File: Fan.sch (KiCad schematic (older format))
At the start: 0 parts

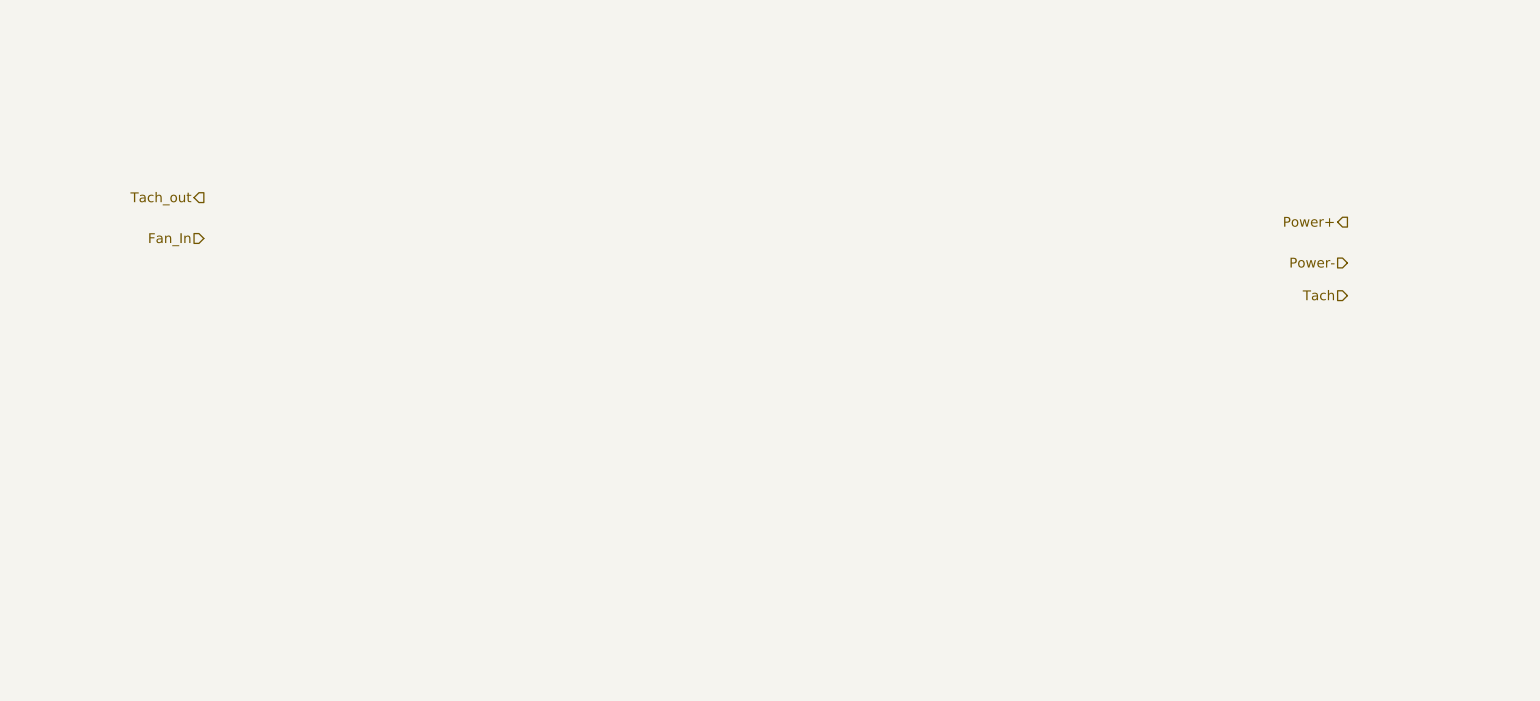
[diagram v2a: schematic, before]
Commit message: Added Fan/Current driver block diagram
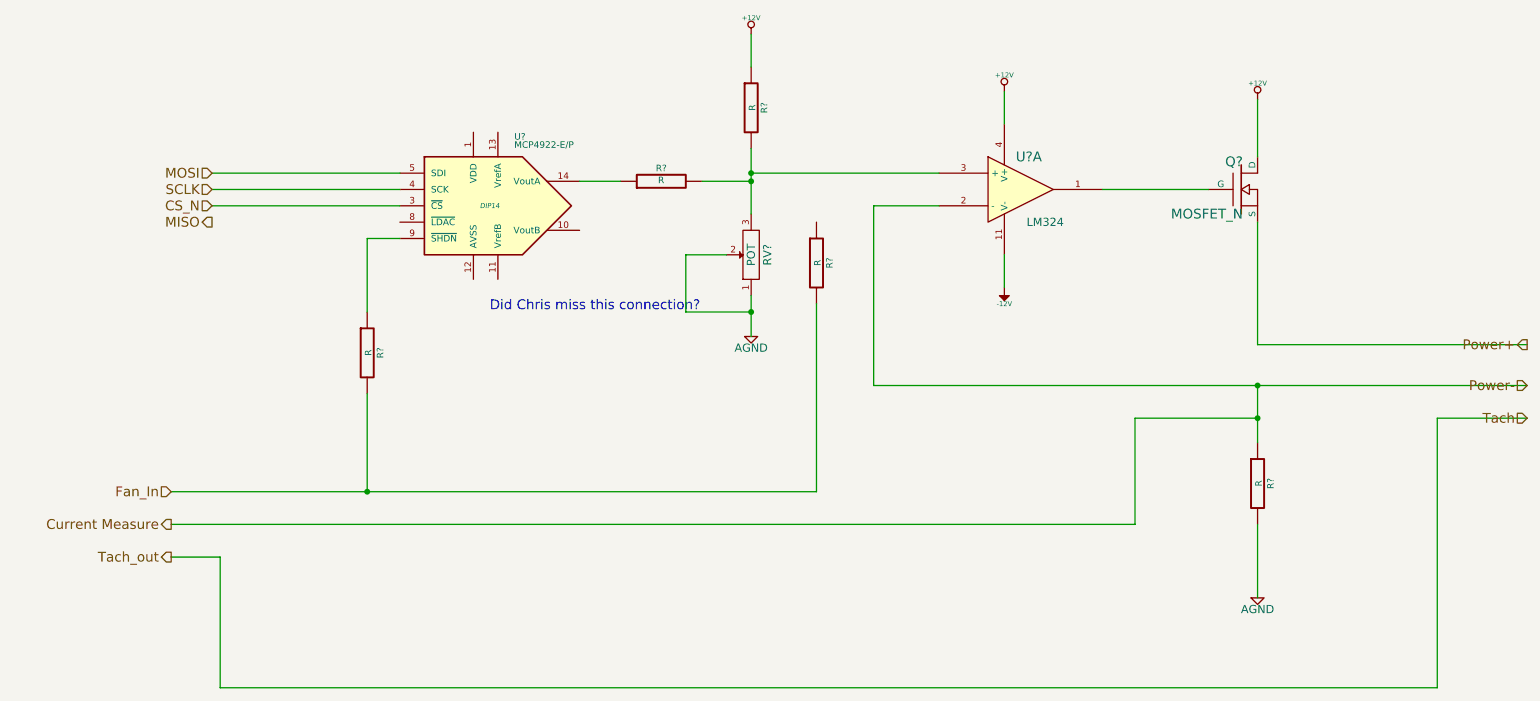
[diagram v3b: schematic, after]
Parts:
- added Q?: MOSFET_N, ~, symbol MOSFET_N
- added R? (x5): R, ~, symbol R
- added RV?: POT, ~, symbol POT
- added U?: LM324, symbol LM324
- added U?: MCP4922-E/P, DIP14, symbol MCP4922-E/P
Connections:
- net Fan_In: now also R?.2, R?.2
- net Power+: now also Q?.S
- new net: Q?.G, U?.1
- new net: R?.2, R?.2, RV?.3, U?.3 (+)
- new net: R?.1, U?.14 (VoutA)
- new net: R?.1, U?.9 (~SHDN~)
- new net +12V: Q?.D, R?.1, U?.4 (V+)
- new net -12V: U?.11 (V-)
- new net AGND: R?.2, RV?.1, RV?.2
- new net CS_N: U?.3 (~CS~)
- new net Current Measure: R?.1, U?.2 (-)
- new net MOSI: U?.5 (SDI)
- new net SCLK: U?.4 (SCK)
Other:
- note added: "Did Chris miss this connection?"

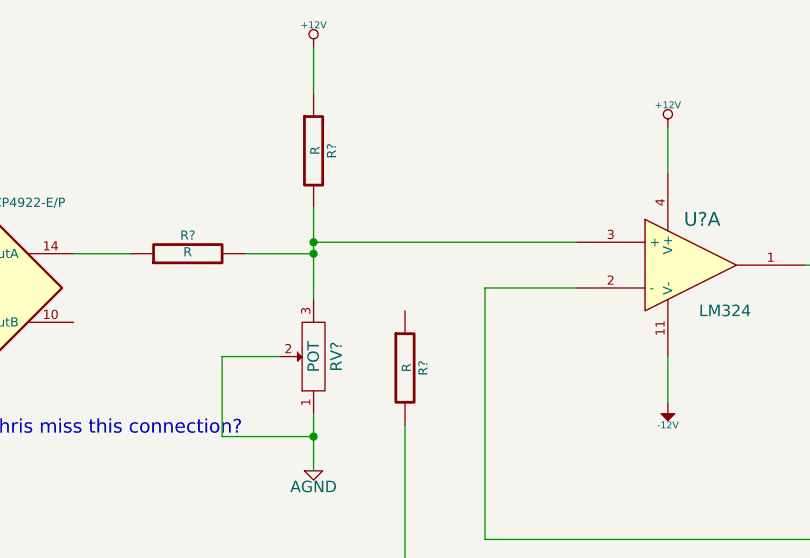
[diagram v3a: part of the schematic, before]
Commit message: Added missing wire for fan disable
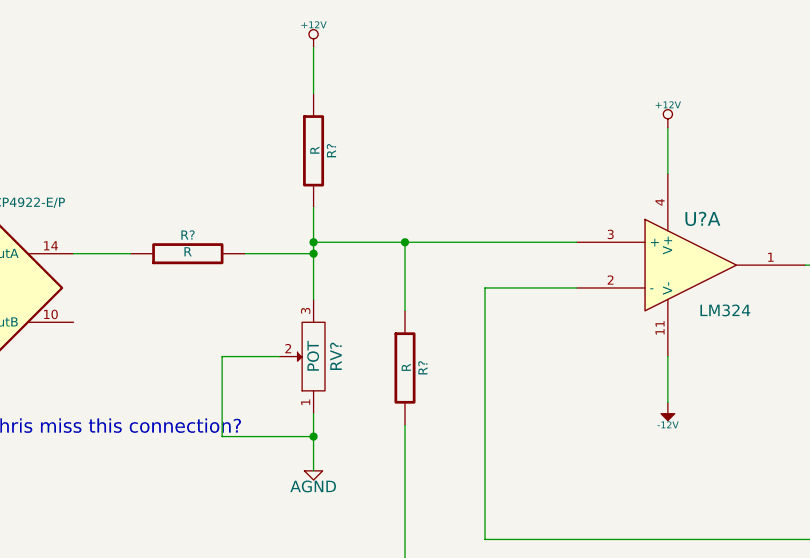
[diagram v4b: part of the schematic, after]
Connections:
- net at R?.2, R?.2, RV?.3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: now also R?.1
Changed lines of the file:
@@
 Text Notes 3700 3000 0    60   ~ 0
 Did Chris miss this connection?
+Wire Wire Line
+	5700 2450 5700 2150
+Connection ~ 5700 2150
 $EndSCHEMATC

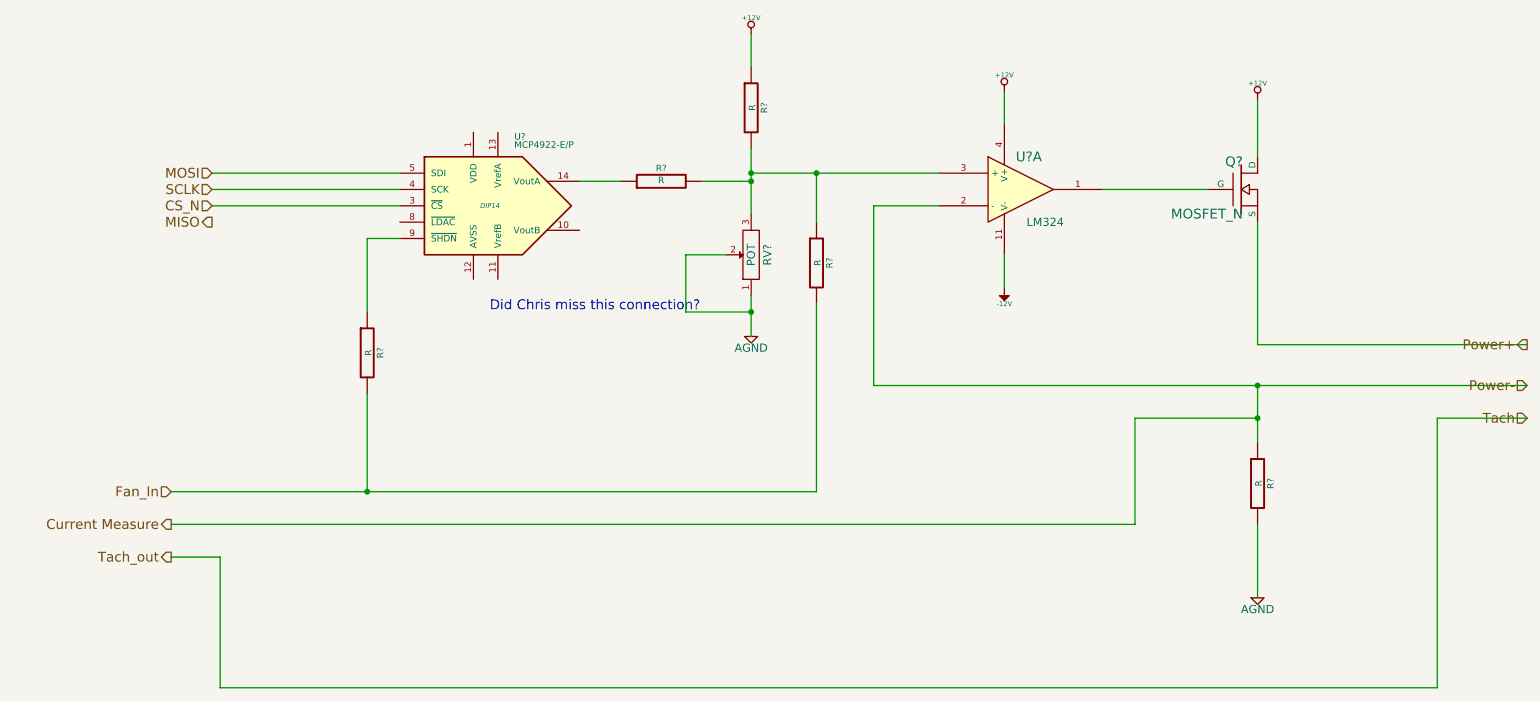
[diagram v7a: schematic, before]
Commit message: Added Arduino Block
Added Arduino Block and connected the top level of the schematic.
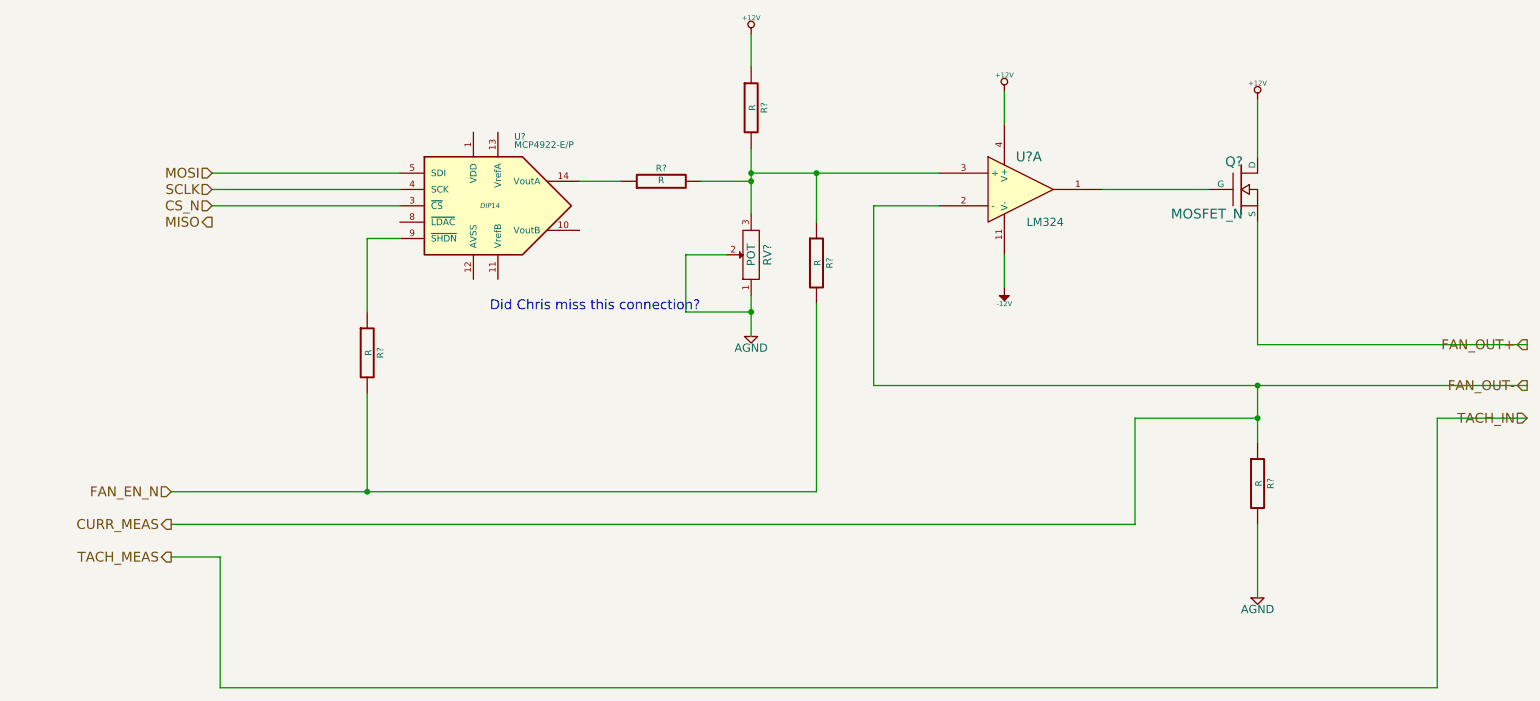
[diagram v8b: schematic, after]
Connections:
- net Current Measure renamed CURR_MEAS
- net Fan_In renamed FAN_EN_N
- net Power+ renamed FAN_OUT+
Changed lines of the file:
@@
 $Descr A4 11693 8268
 encoding utf-8
-Sheet 7 9
+Sheet 6 9
 Title ""
 Date "28 sep 2013"
@@
 $EndDescr
 Text HLabel 10050 3200 0    60   Output ~ 0
-Power+
-Text HLabel 10050 3450 0    60   Input ~ 0
-Power-
+FAN_OUT+
+Text HLabel 10050 3450 0    60   Output ~ 0
+FAN_OUT-
 Text HLabel 10050 3650 0    60   Input ~ 0
-Tach
+TACH_IN
 Text HLabel 1750 4500 0    60   Output ~ 0
-Tach_out
+TACH_MEAS
 Text HLabel 1750 4100 0    60   Input ~ 0
-Fan_In
+FAN_EN_N
 $Comp
 L LM324 U?
@@
 	2050 4500 1750 4500
 Text HLabel 1750 4300 0    60   Output ~ 0
-Current Measure
+CURR_MEAS
 Wire Wire Line
 	8400 3650 7650 3650
